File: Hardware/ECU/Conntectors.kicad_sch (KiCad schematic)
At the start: 2 parts, among them J2 Delphi_Sicma_24, J3 Delphi_Sicma_24

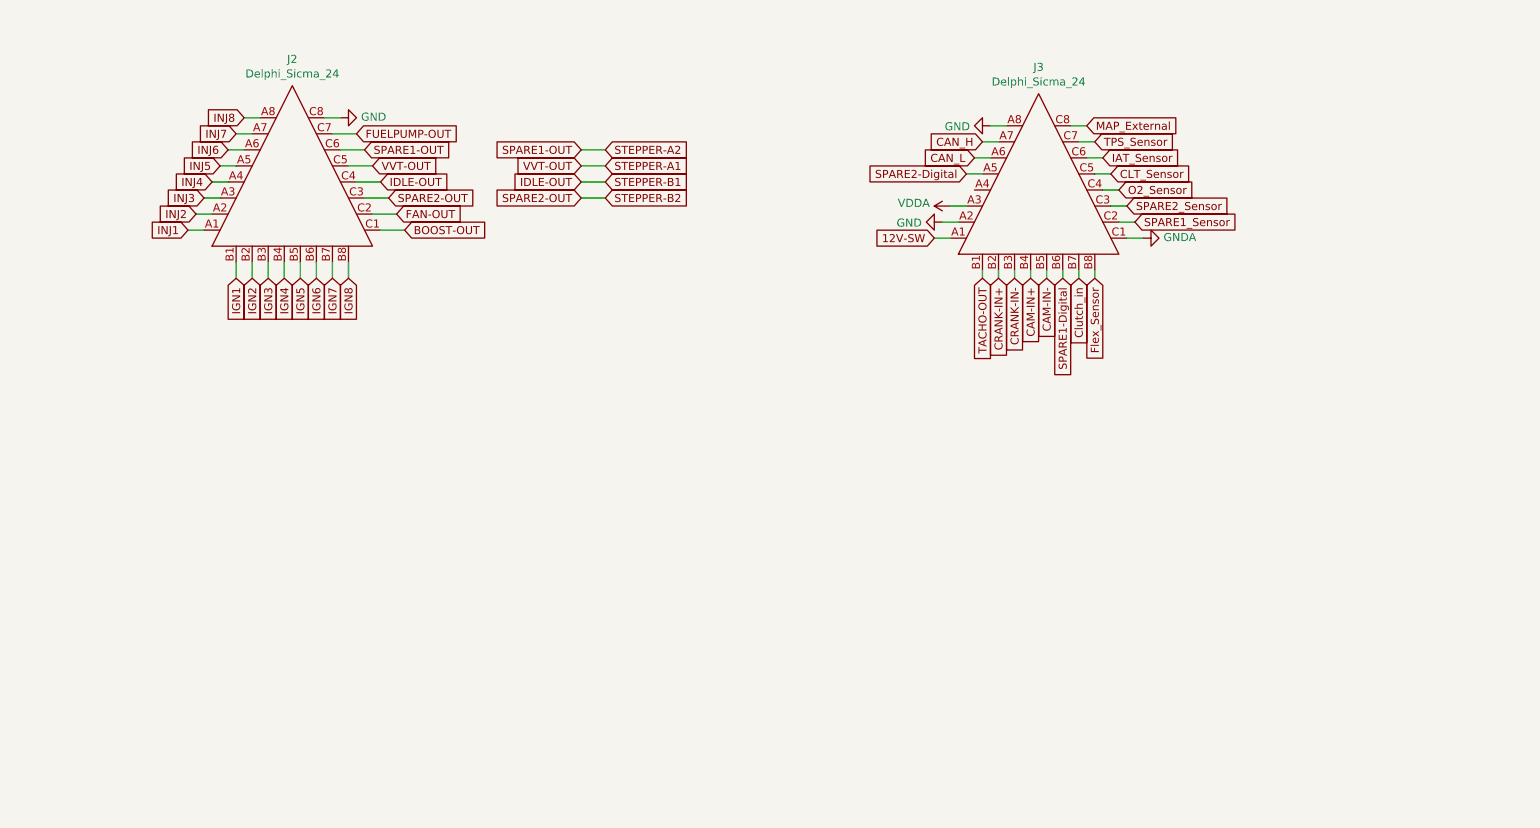
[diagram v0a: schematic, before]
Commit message: Aktualisiere Subprojekt-Commit und füge neue Bibliotheken sowie Anpassungen in der ECU-Konfiguration hinzu
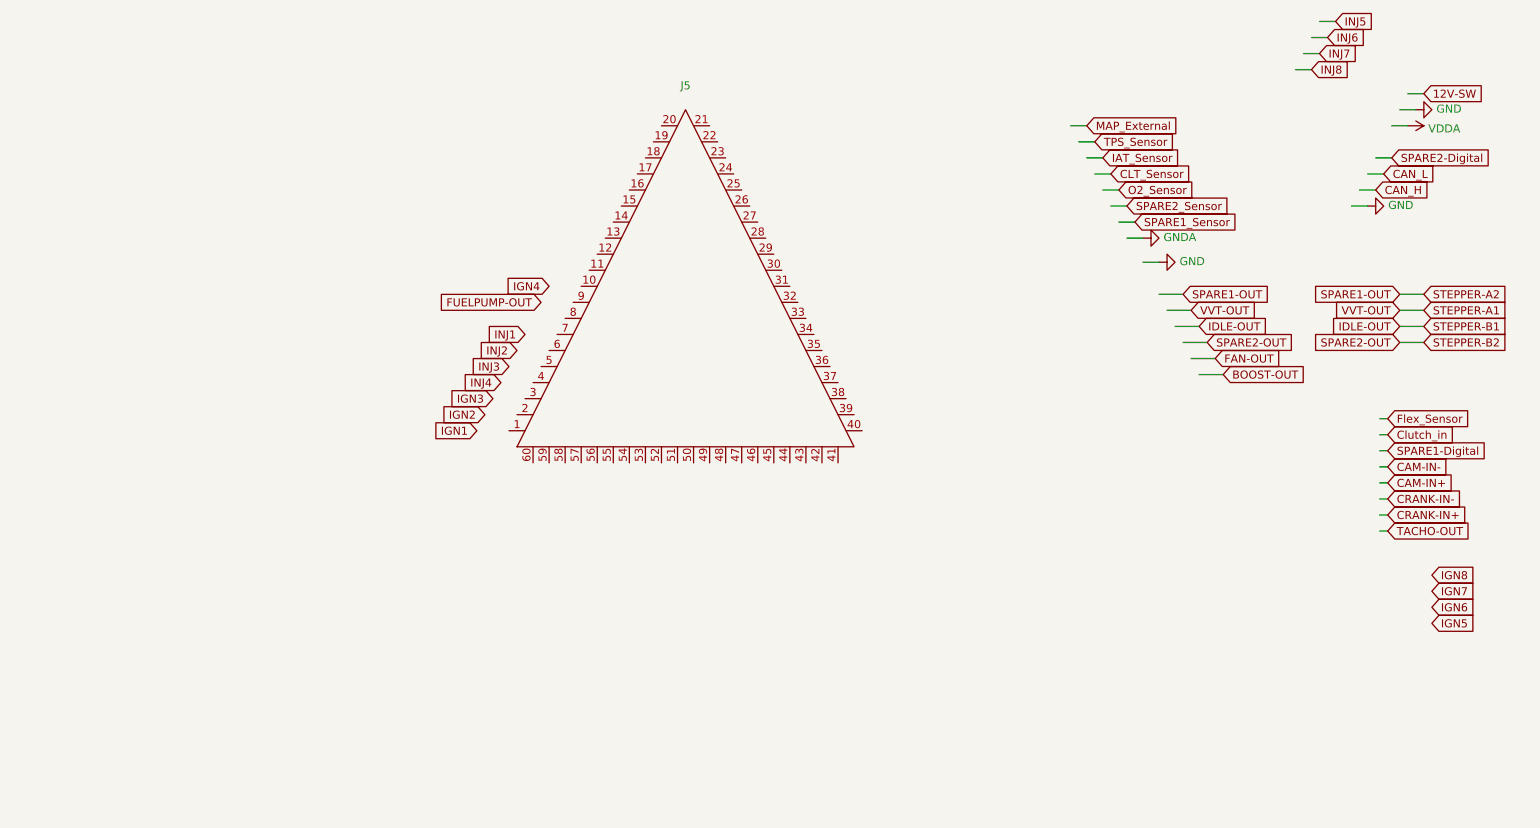
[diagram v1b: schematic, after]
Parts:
- removed J2: Delphi_Sicma_24, Connector_Automotive:Delphi_Sicma_24_Grey, symbol Connector_Automotive:Delphi_Sicma_24
- removed J3: Delphi_Sicma_24, Connector_Automotive:Delphi_Sicma_24_Black, symbol Connector_Automotive:Delphi_Sicma_24
- added J5: ~, connector:6437288-3, symbol connector:6437288-3

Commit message: modified:   Hardware/ECU/Conntectors.kicad_sch 	deleted:    Hardware/ECU/ECU-backups/ECU-2024-10-31_195121.zip 	deleted:    Hardware/ECU/ECU-backups/ECU-2024-10-31_200337.zip 	deleted:    Hardware/ECU/ECU-backups/ECU-2024-10-31_204750.zip 	deleted:    Hardware/ECU/ECU-backups/ECU-2024-10-31_205306.zip 	deleted:    Hardware/ECU/ECU-backups/ECU-2024-10-31_224509.zip 	deleted:    Hardware/ECU/ECU-backups/ECU-2024-11-01_010106.zip 	deleted:    Hardware/ECU/ECU-backups/ECU-2024-11-05_092146.zip 	modified:   Hardware/ECU/ECU.kicad_sch 	deleted:    Hardware/ECU/docs/0900766b80fa0058.pdf:Zone.Identifier 	deleted:    Hardware/ECU/docs/155849888-9-6437288-3.zip:Zone.Identifier 	deleted:    Hardware/ECU/docs/155850325-21-6437288-3.zip:Zone.Identifier 	deleted:    Hardware/ECU/docs/ECM-pinout.pdf 	deleted:    docs/08ecubusapinout.jpg 	deleted:    docs/suzuki-gsx-1300-r-hayabusa-1999-2003-service-manual.pdf:Zone.Identifier 	modified:   speeduino 	Hardware/ECU/ECU-backups/ECU-2024-12-18_220608.zip 	Hardware/ECU/ECU-backups/ECU-2024-12-30_215431.zip 	Hardware/ECU/ECU-backups/ECU-2024-12-31_001349.zip 	Hardware/ECU/ECU-backups/ECU-2025-01-02_140333.zip 	Hardware/ECU/ECU-backups/ECU-2025-01-02_142840.zip 	Hardware/ECU/ECU-backups/ECU-2025-01-02_150227.zip 	Hardware/ECU/ECU-backups/ECU-2025-01-03_004705.zip 	Hardware/ECU/ECU-backups/ECU-2025-01-03_005407.zip 	Hardware/ECU/ECU-backups/ECU-2025-01-03_013204.zip 	Hardware/ECU/ECU-backups/ECU-2025-01-03_020554.zip 	Hardware/ECU/docs/Pinout.ods
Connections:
- net 12V-SW: now also J5.17
- net CAM-IN+: now also J5.37
- net CAM-IN-: now also J5.44
- net CLT_Sensor: now also J5.51
- net CRANK-IN+: now also J5.43
- net CRANK-IN-: now also J5.36
- net FUELPUMP-OUT: now also J5.9
- net GND: now also J5.18, J5.21, J5.26, J5.27, J5.35
- net GNDA: now also J5.54
- net IAT_Sensor: now also J5.50
- net IGN1: now also J5.1
- net IGN2: now also J5.2
- net IGN3: now also J5.3
- net IGN4: now also J5.10
- net INJ1: now also J5.7
- net INJ2: now also J5.6
- net INJ3: now also J5.5
- net INJ4: now also J5.4
- net TACHO-OUT: now also J5.55
- net TPS_Sensor: now also J5.49
- net VDDA: now also J5.48
- net NC: now reaches J5.11
- net NC: now also J5.12, J5.13, J5.14, J5.29, J5.30, J5.31, J5.32, J5.33, J5.34, J5.38, J5.39, J5.40, J5.41, J5.45, J5.46, J5.47, J5.53
- net USB 5V: now reaches J5.16
- net Starter Relay Input: now reaches J5.19
- net Neutral input: now reaches J5.20
- net Diagnose Stecker: now reaches J5.22
- net USB D-: now reaches J5.23
- net USB GND: now reaches J5.24
- net USB D+: now reaches J5.25
- net Starter Relay: now reaches J5.28
- net Tacho Data: now reaches J5.56
- net Unterdruck Steuer Magnetventil: now reaches J5.8

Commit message: update to Kicad v9
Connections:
- net Unterdruck Steuer Magnetventil is gone; now on net IDLE-OUT: J5.8
- net Flex_Sensor: now also J5.39
- net MAP_External: now also J5.58
- net O2_Sensor: now also J5.38
- net SPARE2-OUT: now also J5.11, J5.12, J5.13, J5.14, J5.29, J5.30, J5.31, J5.32, J5.33, J5.34, J5.40, J5.41, J5.45, J5.46, J5.47, J5.53
- removed net NC: J5.11, J5.12, J5.13, J5.14, J5.29, J5.30, J5.31, J5.32, J5.33, J5.34, J5.38, J5.39, J5.40, J5.41, J5.45, J5.46, J5.47, J5.53
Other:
- note added: "Spannungsteiler mit pulldown teiler 22kohm 10kohm ? 3,4V pulldown 100kohm"

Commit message: PCB
Platine Vernetzt
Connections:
- net BOOST-OUT: now also J5.30
- net CAN_H: now also J5.14
- net CAN_L: now also J5.15
- net FAN-OUT: now also J5.29
- net SPARE1-OUT: now also J5.31
- net SPARE1_Sensor: now also J5.57
- net SPARE2-Digital: now also J5.60
- net SPARE2-OUT: no longer J5.11, J5.12, J5.13, J5.14, J5.29, J5.30, J5.31, J5.33, J5.34, J5.40, J5.41, J5.45, J5.46, J5.47, J5.53
- net SPARE2_Sensor: now also J5.53
- net Fuel pump FB: now reaches J5.42
- net Static_Air: now reaches J5.52
- net Tip Over Sensor: now reaches J5.59
- net MAP_External renamed Baro_Sensor
- net Starter Relay renamed Starter Relay FB
- new net NC: J5.11, J5.12, J5.13, J5.33, J5.34, J5.40, J5.41, J5.46, J5.47
- new net O2-Heater: J5.45

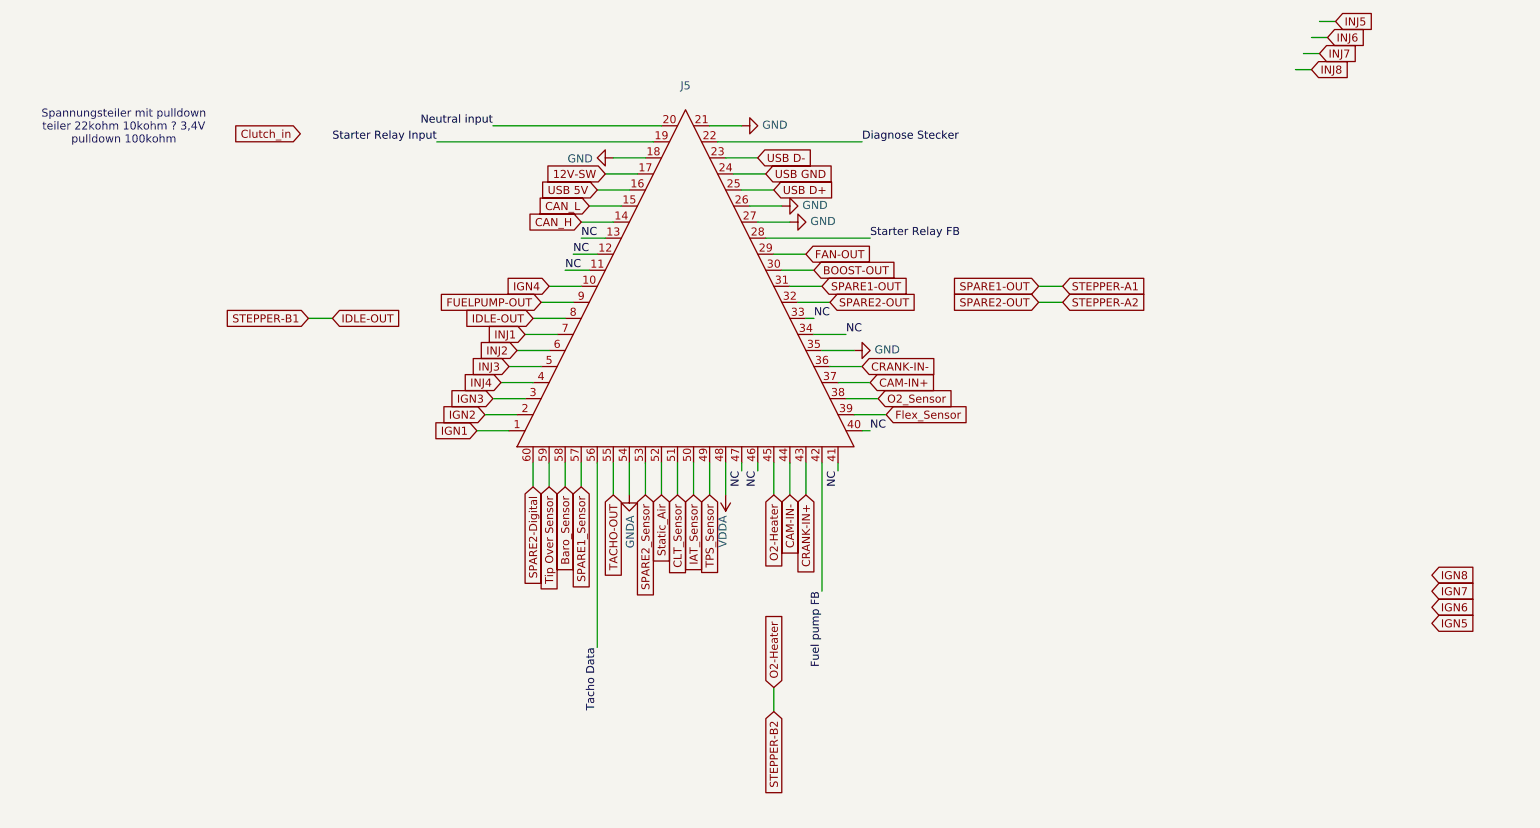
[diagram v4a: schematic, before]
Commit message: PCB v0.2
leiterbahndicke updated
Clutch input rework
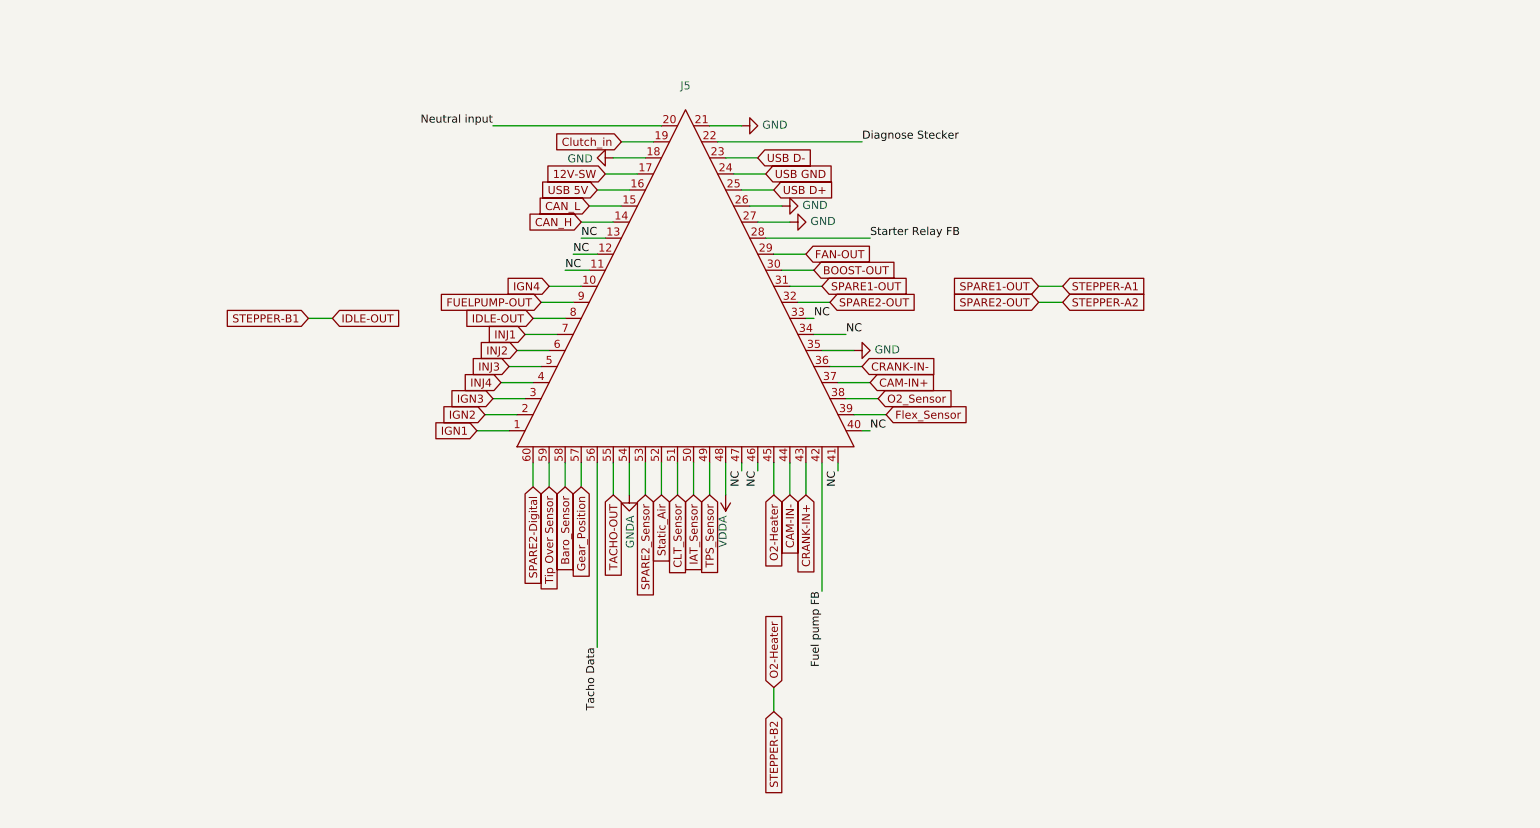
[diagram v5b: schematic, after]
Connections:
- net Starter Relay Input is gone; now on net Clutch_in: J5.19
- net SPARE1_Sensor renamed Gear_Position
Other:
- note removed: "Spannungsteiler mit pulldown teiler 22kohm 10kohm ? 3,4V pulldown 100kohm"

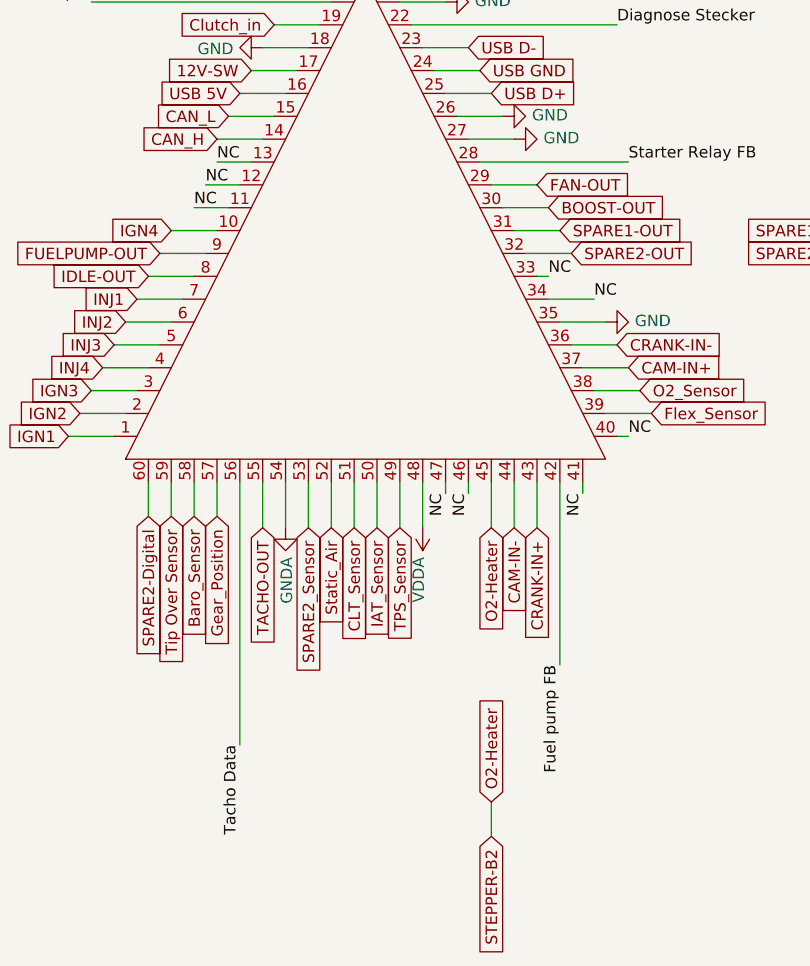
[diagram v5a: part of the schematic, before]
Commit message: modified:   Hardware/ECU/Conntectors.kicad_sch deleted:    Hardware/ECU/ECU-backups/ECU-2025-05-14_000421.zip deleted:    Hardware/ECU/ECU-backups/ECU-2025-05-14_001426.zip deleted:    Hardware/ECU/ECU-backups/ECU-2025-05-14_002531.zip deleted:    Hardware/ECU/ECU-backups/ECU-2025-05-14_003555.zip deleted:    Hardware/ECU/ECU-backups/ECU-2025-05-14_004055.zip modified:   Hardware/ECU/ECU.kicad_pcb modified:   Hardware/ECU/ECU.kicad_prl modified:   Hardware/ECU/ECU.kicad_pro modified:   Hardware/ECU/ECU.kicad_sch 	modified:   Hardware/ECU/Inputs.kicad_sch 	modified:   Hardware/ECU/Inputs2.kicad_sch 	modified:   Hardware/ECU/Schematics.pdf 	modified:   Hardware/ECU/docs/Pinout.ods 	Hardware/ECU/ECU-backups/ECU-2025-05-19_135220.zip 	Hardware/ECU/ECU-backups/ECU-2025-05-19_140656.zip 	Hardware/ECU/ECU-backups/ECU-2025-05-19_142320.zip 	Hardware/ECU/ECU-backups/ECU-2025-05-19_145225.zip 	Hardware/ECU/ECU-backups/ECU-2025-05-19_160311.zip 	Hardware/ECU/ECU.kicad_pcb.zip 	Hardware/ECU/docs/GPS.JPG 	docs/Kabelplan.pdn
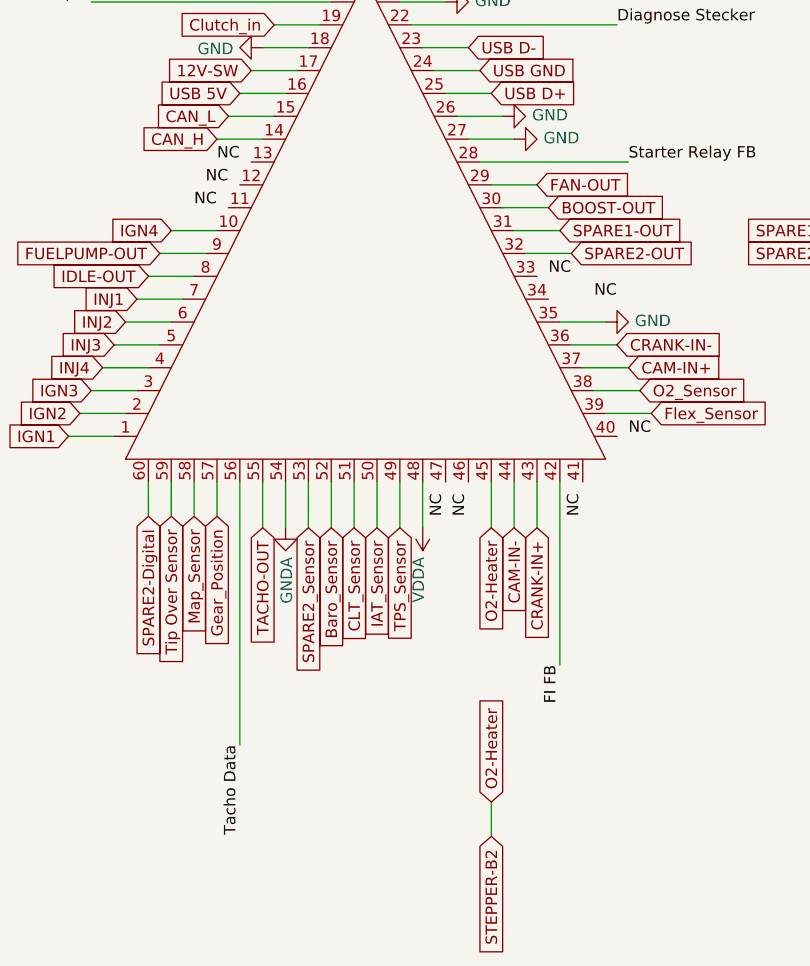
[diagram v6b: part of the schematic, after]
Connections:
- net Static_Air is gone; now on net Baro_Sensor: J5.52
- net Baro_Sensor: no longer J5.58
- net NC: no longer J5.11, J5.12, J5.13, J5.33, J5.34, J5.40, J5.41, J5.46, J5.47
- net Fuel pump FB renamed FI FB
- new net Map_Sensor: J5.58
